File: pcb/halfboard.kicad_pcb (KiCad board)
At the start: 2 copper layers, 117.4 x 87.9 mm, 78 parts, among them SW1 SW_PUSH, SW10 SW_PUSH, SW11 SW_PUSH, SW12 SW_PUSH, SW13 SW_PUSH, SW14 SW_PUSH, SW15 SW_PUSH, SW16 SW_PUSH, SW17 SW_PUSH, SW18 SW_PUSH, SW19 SW_PUSH, SW2 SW_PUSH, SW20 SW_PUSH, SW21 SW_PUSH, SW22 SW_PUSH, SW23 SW_PUSH, SW24 SW_PUSH, SW3 SW_PUSH, SW4 SW_PUSH, SW5 SW_PUSH, SW6 SW_PUSH, SW7 SW_PUSH, SW8 SW_PUSH, SW9 SW_PUSH, U1 ProMicro

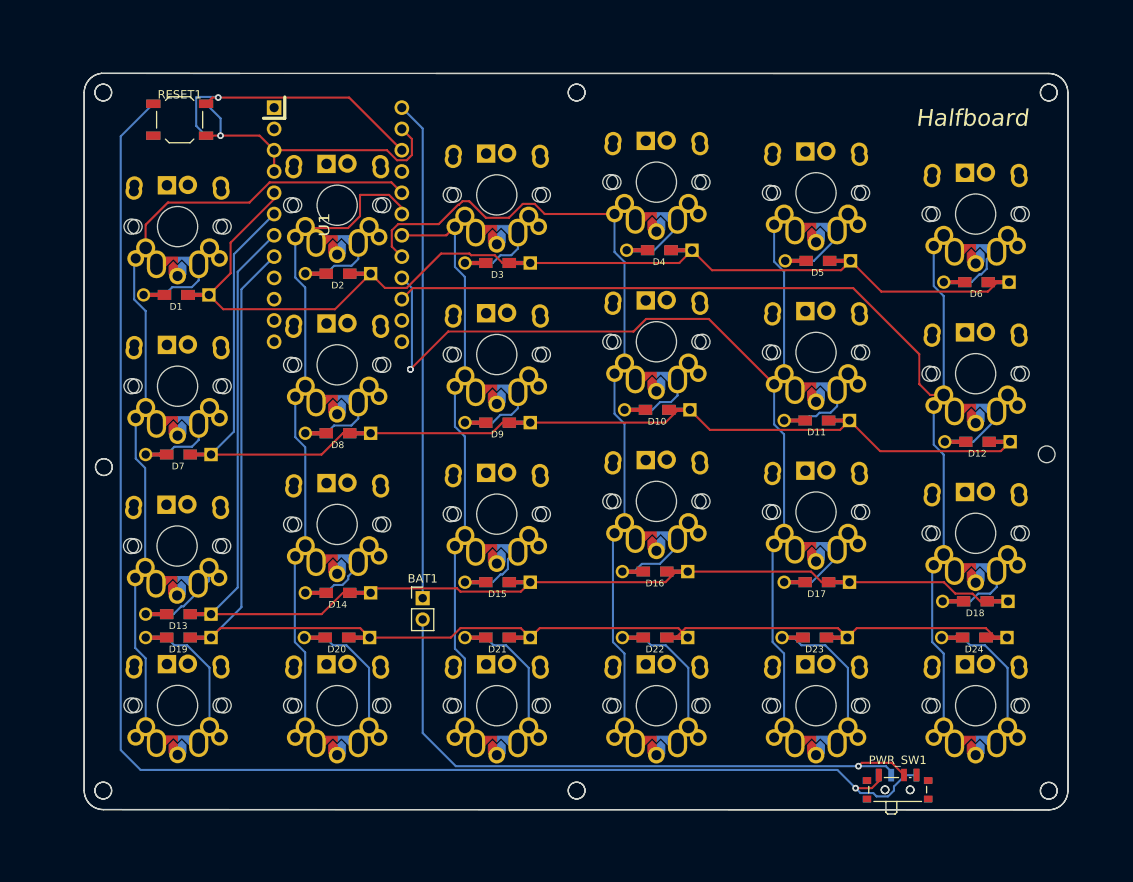
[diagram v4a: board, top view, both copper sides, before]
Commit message: add ground plane
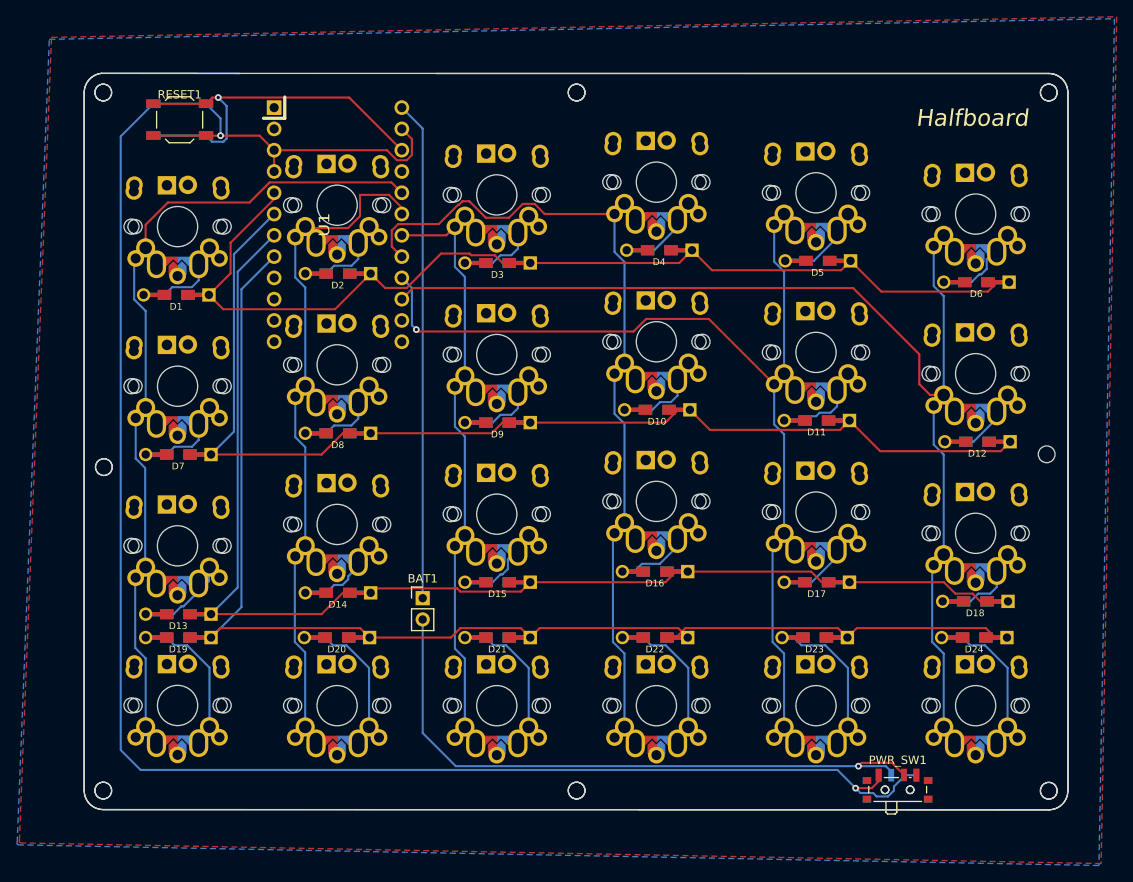
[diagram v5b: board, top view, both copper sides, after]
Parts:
- removed the   at (99.2, 87.9)
- removed the   at (156.4, 101.6)
- removed the   at (118.3, 104.4)
- removed the   at (175.4, 83.8)
- removed the   at (194.5, 126.0)
- removed the   at (118.3, 126.0)
- removed the   at (156.4, 63.5)
- removed the   at (137.3, 65.0)
- removed the   at (175.4, 102.9)
- removed the   at (99.2, 106.9)
- removed the   at (156.4, 82.6)
- removed the   at (99.2, 126.0)
- removed the   at (118.3, 85.3)
- removed the   at (118.3, 66.3)
- removed the   at (175.4, 126.0)
- removed the   at (194.5, 86.4)
- removed the   at (137.3, 84.1)
- removed the   at (156.4, 126.0)
- removed the   at (194.5, 67.3)
- removed the   at (137.3, 103.1)
- removed the   at (99.2, 68.8)
- removed the   at (175.4, 64.8)
- removed the   at (137.3, 126.0)
- moved SW13 0.06 mm to (99.2, 106.9)
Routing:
- net col2: track 65.4 -> 82.4 mm
- net col5: track 129.1 -> 146.1 mm
- net col1: track 73.6 -> 90.6 mm
- net col0: track 90.9 -> 107.9 mm
- net col3: track 94.0 -> 111.0 mm
- net reset: track 34.0 -> 47.2 mm
- net GND: track 218.1 -> 230.8 mm
- net col4: track 119.7 -> 129.6 mm, vias 2 -> 1
- net Net-(D11-Pad2): track 6.45 -> 10.7 mm
- net Net-(D5-Pad2): track 5.69 -> 9.94 mm
- net Net-(D14-Pad2): track 5.83 -> 10.1 mm
- net Net-(D13-Pad2): track 8.47 -> 12.7 mm
- net Net-(D18-Pad2): track 6.58 -> 10.8 mm
- net Net-(D15-Pad2): track 7.11 -> 11.4 mm
- net Net-(D8-Pad2): track 6.46 -> 10.7 mm
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- added copper zone on B.Cu, net (none)
- added copper zone on F.Cu, net (none)

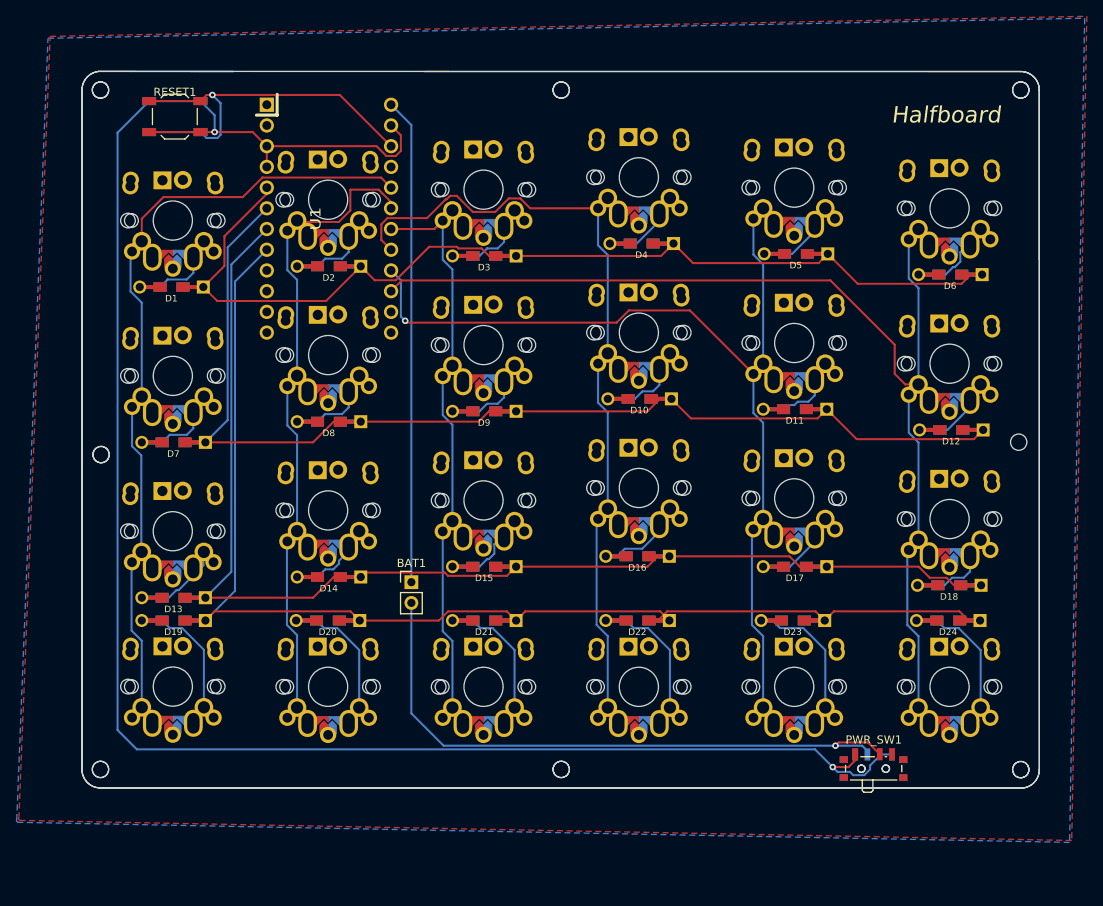
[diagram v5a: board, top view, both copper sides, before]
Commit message: 5x4 layout instead of 6x4
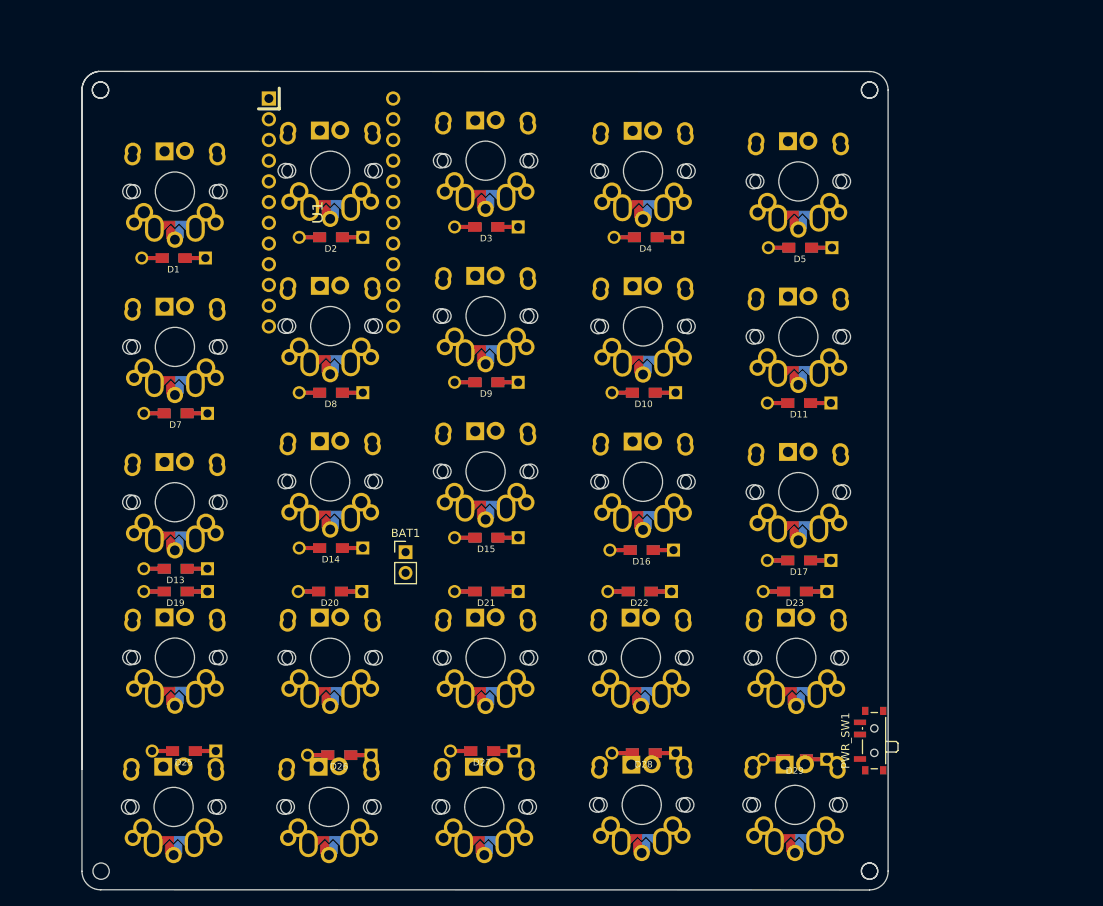
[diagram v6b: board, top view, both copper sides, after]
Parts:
- removed  : , halfboard:MX-ALPs-PG1350-LED-FLIP-PLATE
- removed D12, D18, D24, D6: 1N4148W, halfboard:Diode-dual
- removed PWR_SW2: SW_SPST, Button_Switch_SMD:SW_SPDT_PCM12
- removed RESET1, RESET2: SW_PUSH, Button_Switch_SMD:SW_SPST_TL3342
- removed SW12, SW18, SW24, SW6: SW_PUSH, halfboard:MX-ALPs-PG1350-LED-FLIP
- added D25: 1N4148W, halfboard:Diode-dual, F.Cu at (100.6, 133.9)
- added D26: 1N4148W, halfboard:Diode-dual, F.Cu at (119.6, 134.4)
- added D27: 1N4148W, halfboard:Diode-dual, F.Cu at (137.2, 133.9)
- added D28: 1N4148W, halfboard:Diode-dual, F.Cu at (157.0, 134.1)
- added D29: 1N4148W, halfboard:Diode-dual, F.Cu at (175.5, 134.9)
- added SW25: SW_PUSH, halfboard:MX-ALPs-PG1350-LED-FLIP, F.Cu at (99.3, 140.7)
- added SW26: SW_PUSH, halfboard:MX-ALPs-PG1350-LED-FLIP, F.Cu at (118.4, 140.7)
- added SW27: SW_PUSH, halfboard:MX-ALPs-PG1350-LED-FLIP, F.Cu at (137.4, 140.7)
- added SW28: SW_PUSH, halfboard:MX-ALPs-PG1350-LED-FLIP, F.Cu at (156.7, 140.5)
- added SW29: SW_PUSH, halfboard:MX-ALPs-PG1350-LED-FLIP, F.Cu at (175.5, 140.5)
- moved BAT1 3.75 mm to (127.8, 109.5)
- moved SW15 3.57 mm to (137.6, 99.6)
- moved SW21 3.57 mm to (137.6, 122.4)
- moved SW14 3.57 mm to (118.5, 100.8)
- moved D14 3.57 mm to (118.6, 109.0)
- moved SW13 3.57 mm to (99.5, 103.4)
- moved SW22 3.57 mm to (156.6, 122.4)
- moved SW23 3.57 mm to (175.7, 122.4)
- moved SW3 3.57 mm to (137.6, 61.5)
- moved D15 3.57 mm to (137.7, 107.7)
- moved D21 3.57 mm to (137.7, 114.3)
- moved D23 3.57 mm to (175.5, 114.3)
- moved D3 3.57 mm to (137.7, 69.6)
- moved D9 3.57 mm to (137.7, 88.6)
- moved SW9 3.57 mm to (137.6, 80.5)
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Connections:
- U1 pad 15: col5 -> Net-(U1-Pad15)
- U1 pad 9: Net-(U1-Pad9) -> row4
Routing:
- net GND: track 230.8 -> 0.00 mm, vias 2 -> 0
- net row3: track 149.6 -> 0.00 mm
- net col5: track 146.1 -> 0.00 mm
- net row2: track 146.0 -> 0.00 mm
- net row1: track 130.0 -> 0.00 mm
- net col4: track 129.6 -> 0.00 mm, vias 1 -> 0
- net row0: track 118.9 -> 0.00 mm
- net col3: track 111.0 -> 0.00 mm
- net col0: track 107.9 -> 0.00 mm
- net col1: track 90.6 -> 0.00 mm
- net col2: track 82.4 -> 0.00 mm
- net Net-(BAT1-Pad2): track 78.0 -> 0.00 mm, vias 1 -> 0
- net bat: track 59.6 -> 0.00 mm
- net reset: track 47.2 -> 0.00 mm, vias 1 -> 0
- net Net-(D23-Pad2): track 19.3 -> 0.00 mm
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- removed copper zone on B.Cu, net (none)
- removed copper zone on F.Cu, net (none)
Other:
- board size 117.4 x 87.9 mm -> 98.9 x 100.4 mm
- board text removed: "Halfboard"
